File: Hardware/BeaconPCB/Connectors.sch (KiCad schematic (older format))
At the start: 2 parts

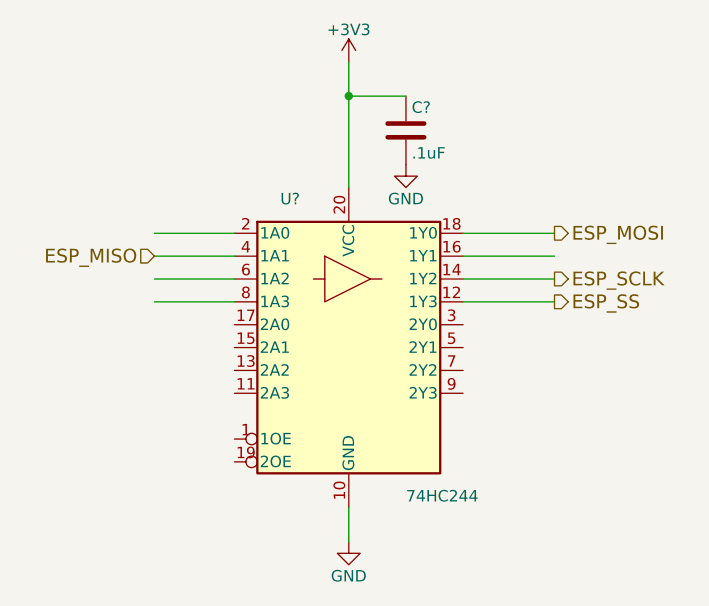
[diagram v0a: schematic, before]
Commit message: Schematic Adjustments
Added 5V power line to Pi header
Adjusted the rest of schematic to use PI SPI lines
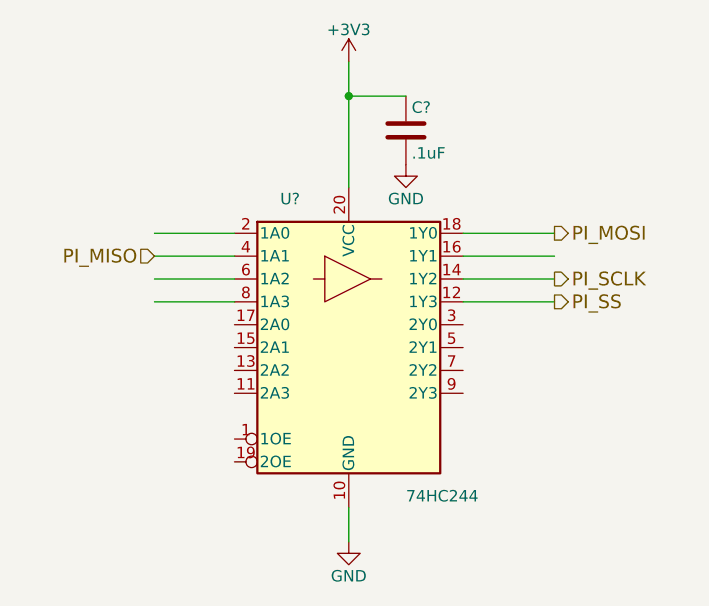
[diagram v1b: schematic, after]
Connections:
- net labels added: PI_MISO, PI_MOSI, PI_SCLK, PI_SS
- net labels removed: ESP_MISO, ESP_MOSI, ESP_SCLK, ESP_SS
- wire segments 12 -> 11
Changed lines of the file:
@@
 Connection ~ 3800 2250
 Wire Wire Line
-	3800 2100 3800 2250
-Wire Wire Line
-	3800 2250 3800 2650
+	3800 2100 3800 2650
 Wire Wire Line
 	4050 2250 3800 2250
@@
 	2950 2850 3300 2850
 Text HLabel 4700 2850 2    60   Output ~ 0
-ESP_MOSI
+PI_MOSI
 Text HLabel 2950 2950 0    60   Input ~ 0
-ESP_MISO
+PI_MISO
 Text HLabel 4700 3050 2    60   Output ~ 0
-ESP_SCLK
+PI_SCLK
 Text HLabel 4700 3150 2    60   Output ~ 0
-ESP_SS
+PI_SS
 $EndSCHEMATC
